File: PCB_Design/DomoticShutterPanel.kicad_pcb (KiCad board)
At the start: 2 copper layers, 110.6 x 50 mm, 62 parts, among them J1 PWR 5V, J10 LCD COM, J2 PWR 5V AUX, J3 TRIGGER SEL, J4 PWR SEL, J5 Screw_Terminal_01x03, J6 RF TX, J7 RF RX, J8 MASTER UART COM, K1 SRD-05VDC-SL-C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

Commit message: Changed to SMD pushbutton
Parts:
- SW1, SW2, SW3, SW4, SW5, SW6: footprint Project_libraries:SW_PUSH_6mm -> Project_libraries:SW_Push_1P1T_NO_6x6mm_H5mm
- moved J8 248.0 mm to (106.3, 78.1), turned to 90 degrees
- moved C1 232.4 mm to (113.3, 82.6), turned to 270 degrees
- moved C2 231.8 mm to (117.1, 83.8), turned to 270 degrees
- moved C3 227.8 mm to (113.1, 87.6)
- moved SW5 226.4 mm to (108.8, 99.7), turned to 90 degrees
- moved SW6 209.7 mm to (101.2, 99.7), turned to 90 degrees
- moved R6 200.3 mm to (108.8, 81.3), turned to 270 degrees
- moved R1 172.5 mm to (164.5, 102.2)
- moved D2 147.7 mm to (186.3, 98.4), turned to 180 degrees
- moved D3 146.6 mm to (176.1, 104.0), turned to 270 degrees
- moved J3 129.8 mm to (162.2, 106.1)
- moved R4 128.1 mm to (171.1, 111.1), turned to 90 degrees
- moved R3 110.7 mm to (181.2, 98.4), turned to 180 degrees
- moved Q1 100.8 mm to (174.6, 118.3), turned to 90 degrees
- moved R2 95.8 mm to (171.1, 118.8), turned to 90 degrees
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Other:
- outline, holes or cut-outs redrawn

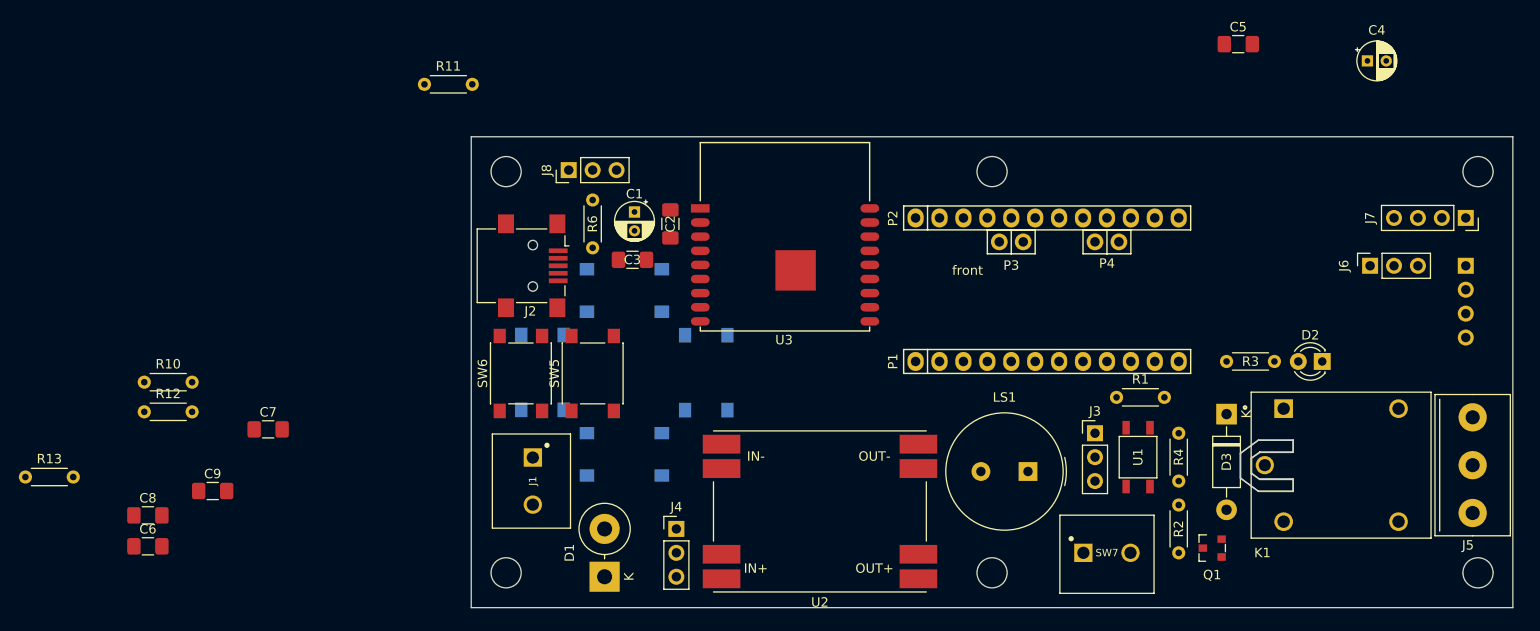
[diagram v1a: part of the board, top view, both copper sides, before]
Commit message: R and C added for buttons
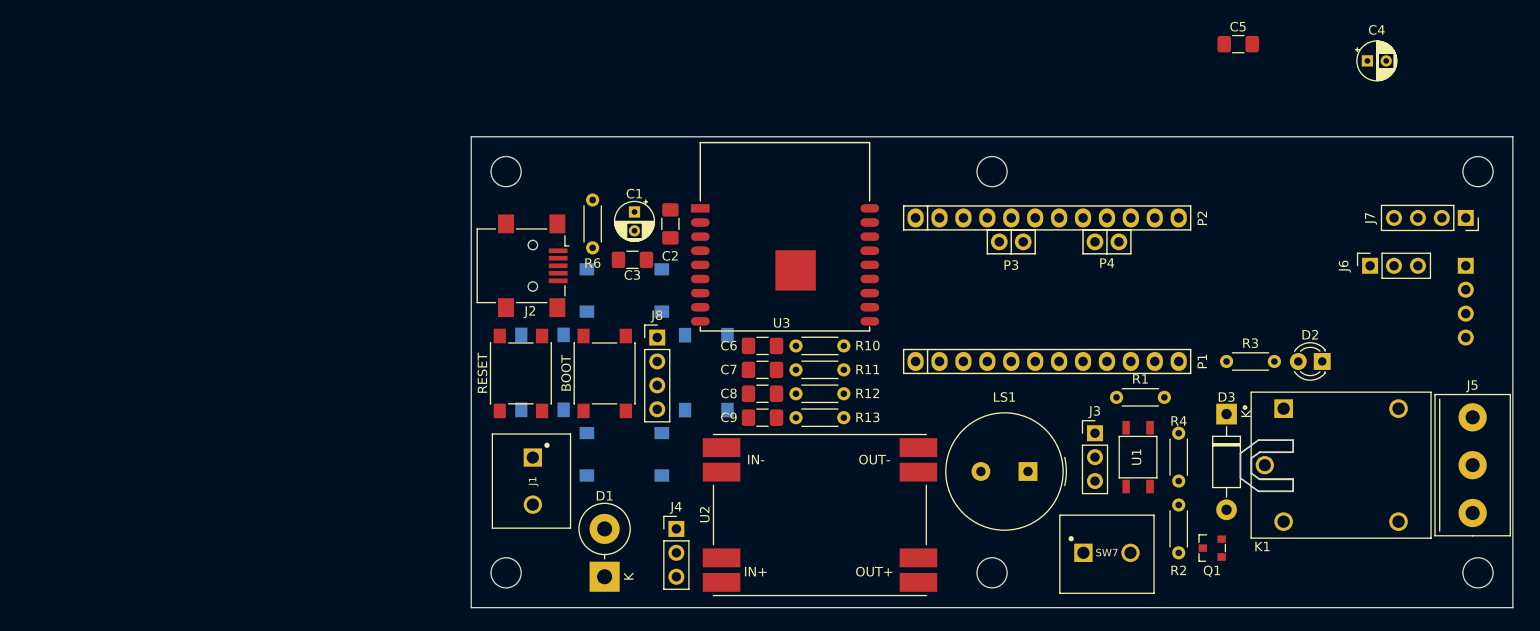
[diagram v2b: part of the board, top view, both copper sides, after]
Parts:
- J8: footprint Connector_PinHeader_2.54mm:PinHeader_1x03_P2.54mm_Vertical -> Connector_PinHeader_2.54mm:PinHeader_1x04_P2.54mm_Vertical
- moved R13 82.1 mm to (130.4, 104.4)
- moved R10 69.3 mm to (130.4, 96.8)
- moved R12 69.2 mm to (130.4, 101.9)
- moved C6 68.6 mm to (126.9, 96.8)
- moved C8 66.5 mm to (126.9, 101.9)
- moved C9 58.9 mm to (126.9, 104.4)
- moved C7 52.9 mm to (126.9, 99.3)
- moved R11 49.8 mm to (130.4, 99.3)
- moved J8 20.1 mm to (115.7, 95.9), turned to 0 degrees
- moved BOOT 1.27 mm to (110.1, 99.7)
- moved U2 0.38 mm to (133.0, 114.7)
- renumbered SW5 to BOOT, SW6 to RESET
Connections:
- J8 pad 2: U1_TXD -> +3V3
- J8 pad 3: U1_RXD -> U1_TXD
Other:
- board text removed: "front"

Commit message: Positioned all footprints
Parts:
- moved C10 213.9 mm to (115.4, 95.4), turned to 270 degrees
- moved C11 210.8 mm to (138.5, 97.2), turned to 180 degrees
- moved R5 181.5 mm to (118.7, 92.9), turned to 90 degrees
- moved R15 178.4 mm to (137.0, 99.3), turned to 270 degrees
- moved C12 175.7 mm to (174.1, 96.2), turned to 90 degrees
- moved R7 167.3 mm to (153.8, 83.7), turned to 180 degrees
- moved D4 166.6 mm to (158.9, 83.7), turned to 180 degrees
- moved R14 151.7 mm to (115.4, 98.9), turned to 270 degrees
- moved R16 143.8 mm to (174.1, 84.2), turned to 90 degrees
- moved R9 137.4 mm to (193.9, 97.2), turned to 90 degrees
- moved R8 123.4 mm to (196.5, 97.2), turned to 90 degrees
- moved C4 92.3 mm to (115.7, 119.8), turned to 270 degrees
- moved C5 80.6 mm to (119.5, 120.8), turned to 270 degrees
- moved J9 36.2 mm to (166.5, 82.7), turned to 180 degrees
- moved LS1 35.9 mm to (183.5, 88.3)
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- renumbered SW7 to J9, BOOT to SW5, RESET to SW6
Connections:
- J1 pad 1: Net-(D1-Pad2) -> GND
- J1 pad 2: GND -> Net-(D1-Pad2)
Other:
- board text added: "3V3"
- board text added: "COM"
- board text added: "GND"
- board text added: "NC"
- board text added: "NO"
- board text added: "RXD"
- board text added: "TXD"

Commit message: New design rules
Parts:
- renumbered REF** to Carcasa
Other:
- net class Default: clearance 0.2 -> 0.127; trace_width 0.25 -> 0.127; via_drill 0.4 -> 0.3
- rule trace_clearance: 0.2 -> 0.127
- rule trace_min: 0.2 -> 0.127
- rule via_min_size: 0.4 -> 0.6

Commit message: Traced tracks
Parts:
- moved C4 72.1 mm to (184.5, 98.4), turned to 0 degrees
- moved C5 65.2 mm to (180.7, 98.4), turned to 180 degrees
- moved C12 13.2 mm to (173.6, 82.9), turned to 270 degrees
- moved R16 7.37 mm to (174.1, 91.6), turned to 270 degrees
- moved J4 6.11 mm to (119.0, 117.0), turned to 180 degrees
- moved J3 5.49 mm to (150.2, 112.9), turned to 180 degrees
- moved R6 5.09 mm to (111.6, 86.8), turned to 90 degrees
- moved R7 3.84 mm to (150.0, 84.2)
- moved D4 2.34 mm to (156.6, 84.2)
- moved J9 2.29 mm to (164.2, 82.7)
- moved D2 1.02 mm to (171.1, 118.5)
- moved R3 1.02 mm to (171.1, 113.4)
- moved LS1 0.76 mm to (183.5, 87.5)
- moved D3 0.51 mm to (176.1, 103.5)
- moved J1 0.51 mm to (102.5, 111.6)
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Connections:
- J9 pad 1: GND -> U2_GPIO2
- J9 pad 2: U2_GPIO2 -> GND
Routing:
- net +5V: track 0.00 -> 168.8 mm, vias 0 -> 1
- net +3V3: track 0.00 -> 165.3 mm
- net I2C_SCL: track 0.00 -> 90.4 mm, vias 0 -> 2
- net I2C_SDA: track 0.00 -> 85.2 mm, vias 0 -> 2
- net DATA_Rx: track 0.00 -> 63.1 mm, vias 0 -> 2
- net U1_RST: track 0.00 -> 58.6 mm, vias 0 -> 2
- net U1_GPIO13: track 0.00 -> 53.5 mm
- net U1_GPIO5: track 0.00 -> 47.7 mm, vias 0 -> 3
- net U2_GPIO2: track 0.00 -> 46.3 mm, vias 0 -> 1
- net U1_RXD: track 0.00 -> 43.1 mm, vias 0 -> 1
- net U1_GPIO4: track 0.00 -> 42.7 mm, vias 0 -> 4
- net DATA_Tx: track 0.00 -> 42.7 mm, vias 0 -> 2
- net U1_TXD: track 0.00 -> 42.2 mm, vias 0 -> 1
- net U2_GPIO5: track 0.00 -> 35.4 mm, vias 0 -> 1
- net U1_GPIO12: track 0.00 -> 31.0 mm, vias 0 -> 1
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- added copper zone on B.Cu, net GND
- added copper zone on F.Cu, net GND
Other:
- net class Default: clearance 0.127 -> 0.1778
- rule trace_clearance: 0.127 -> 0.1778
- board text added: "BOOT"
- board text added: "RESET"

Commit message: Ready to production
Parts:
- added G***: LOGO, Project_libraries:MickySim_Logo_6mm, F.Cu at (183.3, 120.8)
- added REF**: OSHW-Logo2_7.3x6mm_SilkScreen, Symbol:OSHW-Logo2_7.3x6mm_SilkScreen, B.Cu at (196.5, 120.8)
- added REF**: KiCad-Logo_5mm_SilkScreen, Symbol:KiCad-Logo_5mm_SilkScreen, B.Cu at (185.5, 120.8)
- moved D1 3.57 mm to (114.7, 120.5)
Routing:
- net Net-(D1-Pad1): track 10.8 -> 5.79 mm
- net +3V3: track 165.3 -> 162.4 mm
- net +5V: track 168.8 -> 171.1 mm
- net Net-(D1-Pad2): track 8.12 -> 9.76 mm
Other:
- board text added: "5V"
- board text added: "ANALOG"
- board text added: "CAUTION 230 VAC"
- board text added: "DIGITAL"
- board text added: "HIGH"
- board text added: "I2C RESISTORS"
- board text added: "LOW"
- board text added: "NO COPPER AREA"
- board text added: "PWR_5V"
- board text added: "PWR_USB"
- board text added: "ROLLER SHUTTER CONTROL BOARD"
- board text added: "RX"
- board text added: "Rev 1.0"
- board text added: "SCL"
- board text added: "SDA"
- board text added: "THIS SIDE BOTTOM"
- board text added: "THIS SIDE UP"
- board text added: "TX"
